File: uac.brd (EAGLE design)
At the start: 160 x 100 mm, 159 parts, among them Q1 2N7002CK4SST, Q2 2N7002CK4SST

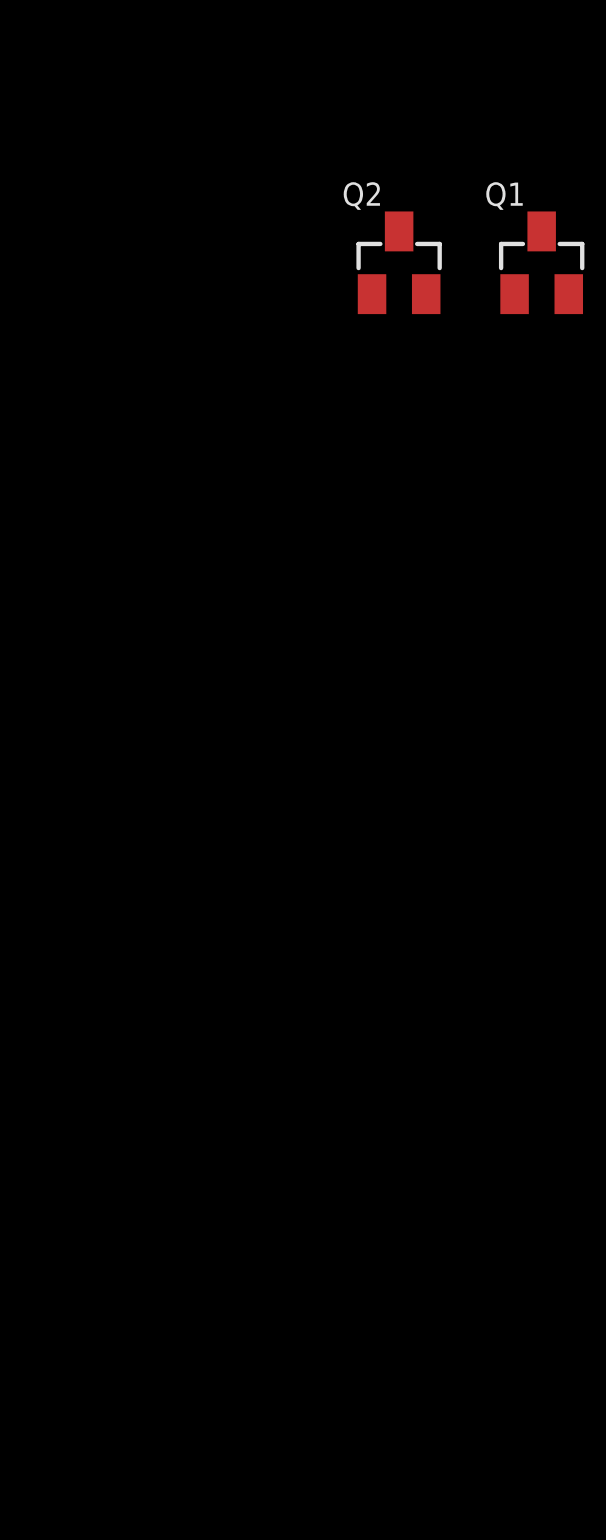
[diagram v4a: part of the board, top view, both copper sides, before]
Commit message: Leds aangesloten
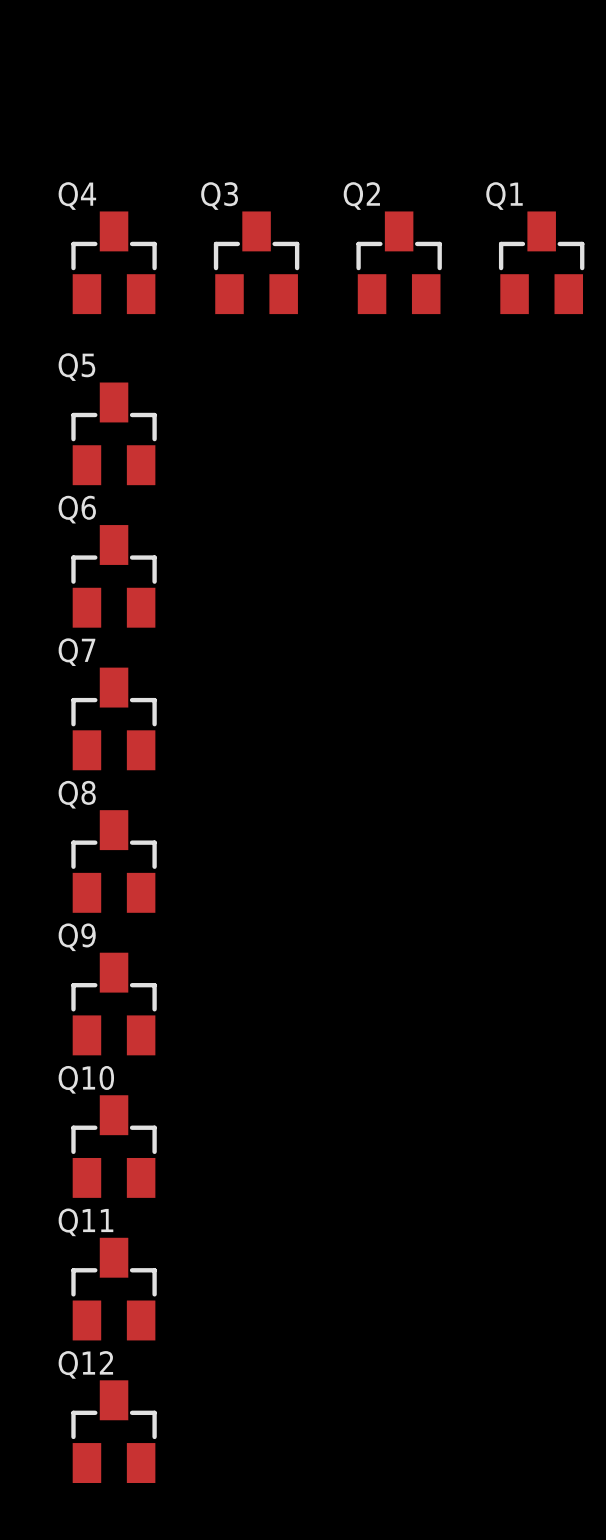
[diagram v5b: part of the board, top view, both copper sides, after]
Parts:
- added Q10, Q11, Q12, Q3, Q4, Q5, Q6, Q7, Q8, Q9: 2N7002CK4SST, Custom components:SOT23
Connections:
- new net ARCDOZEN_10: Q10.1
- new net ARCDOZEN_11: Q11.1
- new net ARCDOZEN_12: Q12.1
- new net ARCDOZEN_3: Q3.1
- new net ARCDOZEN_4: Q4.1
- new net ARCDOZEN_5: Q5.1
- new net ARCDOZEN_6: Q6.1
- new net ARCDOZEN_7: Q7.1
- new net ARCDOZEN_8: Q8.1
- new net ARCDOZEN_9: Q9.1
- new net N$10: HOUR9.C, MIN45.C, MIN46.C, MIN47.C, MIN48.C, MIN49.C, Q10.3, SEC45.C, SEC46.C, SEC47.C, SEC48.C, SEC49.C, SPECIAL9.C
- new net N$11: HOUR10.C, MIN50.C, MIN51.C, MIN52.C, MIN53.C, MIN54.C, Q11.3, SEC50.C, SEC51.C, SEC52.C, SEC53.C, SEC54.C, SPECIAL10.C
- new net N$12: HOUR11.C, MIN55.C, MIN56.C, MIN57.C, MIN58.C, MIN59.C, Q12.3, SEC55.C, SEC56.C, SEC57.C, SEC58.C, SEC59.C, SPECIAL11.C
- new net N$2: HOUR2.C, MIN10.C, MIN11.C, MIN12.C, MIN13.C, MIN14.C, Q3.3, SEC10.C, SEC11.C, SEC12.C, SEC13.C, SEC14.C, SPECIAL2.C
- new net N$4: HOUR3.C, MIN15.C, MIN16.C, MIN17.C, MIN18.C, MIN19.C, Q4.3, SEC15.C, SEC16.C, SEC17.C, SEC18.C, SEC19.C, SPECIAL3.C
- new net N$5: HOUR4.C, MIN20.C, MIN21.C, MIN22.C, MIN23.C, MIN24.C, Q5.3, SEC20.C, SEC21.C, SEC22.C, SEC23.C, SEC24.C, SPECIAL4.C
- new net N$6: HOUR5.C, MIN25.C, MIN26.C, MIN27.C, MIN28.C, MIN29.C, Q6.3, SEC25.C, SEC26.C, SEC27.C, SEC28.C, SEC29.C, SPECIAL5.C
- new net N$7: HOUR6.C, MIN30.C, MIN31.C, MIN32.C, MIN33.C, MIN34.C, Q7.3, SEC30.C, SEC31.C, SEC32.C, SEC33.C, SEC34.C, SPECIAL6.C
- new net N$8: HOUR7.C, MIN35.C, MIN36.C, MIN37.C, MIN38.C, MIN39.C, Q8.3, SEC35.C, SEC36.C, SEC37.C, SEC38.C, SEC39.C, SPECIAL7.C
- new net N$9: HOUR8.C, MIN40.C, MIN41.C, MIN42.C, MIN43.C, MIN44.C, Q9.3, SEC40.C, SEC41.C, SEC42.C, SEC43.C, SEC44.C, SPECIAL8.C
- net DOZEN1: now also HOUR10.A, HOUR11.A, HOUR2.A, HOUR3.A, HOUR4.A, HOUR5.A, HOUR6.A, HOUR7.A, HOUR8.A, HOUR9.A
- net DOZEN10: now also SEC13.A, SEC18.A, SEC23.A, SEC28.A, SEC33.A, SEC38.A, SEC43.A, SEC48.A, SEC53.A, SEC58.A
- net DOZEN11: now also SEC14.A, SEC19.A, SEC24.A, SEC29.A, SEC34.A, SEC39.A, SEC44.A, SEC49.A, SEC54.A, SEC59.A
- net DOZEN12: now also SPECIAL10.A, SPECIAL11.A, SPECIAL2.A, SPECIAL3.A, SPECIAL4.A, SPECIAL5.A, SPECIAL6.A, SPECIAL7.A, SPECIAL8.A, SPECIAL9.A
- net DOZEN2: now also MIN10.A, MIN15.A, MIN20.A, MIN25.A, MIN30.A, MIN35.A, MIN40.A, MIN45.A, MIN50.A, MIN55.A
- net DOZEN3: now also MIN11.A, MIN16.A, MIN21.A, MIN26.A, MIN31.A, MIN36.A, MIN41.A, MIN46.A, MIN51.A, MIN56.A
- net DOZEN4: now also MIN12.A, MIN17.A, MIN22.A, MIN27.A, MIN32.A, MIN37.A, MIN42.A, MIN47.A, MIN52.A, MIN57.A
- net DOZEN5: now also MIN13.A, MIN18.A, MIN23.A, MIN28.A, MIN33.A, MIN38.A, MIN43.A, MIN48.A, MIN53.A, MIN58.A
- net DOZEN6: now also MIN14.A, MIN19.A, MIN24.A, MIN29.A, MIN34.A, MIN39.A, MIN44.A, MIN49.A, MIN54.A, MIN59.A
- net DOZEN7: now also SEC10.A, SEC15.A, SEC20.A, SEC25.A, SEC30.A, SEC35.A, SEC40.A, SEC45.A, SEC50.A, SEC55.A
- net DOZEN8: now also SEC11.A, SEC16.A, SEC21.A, SEC26.A, SEC31.A, SEC36.A, SEC41.A, SEC46.A, SEC51.A, SEC56.A
- net DOZEN9: now also SEC12.A, SEC17.A, SEC22.A, SEC27.A, SEC32.A, SEC37.A, SEC42.A, SEC47.A, SEC52.A, SEC57.A
- net GND: now also Q10.2, Q11.2, Q12.2, Q3.2, Q4.2, Q5.2, Q6.2, Q7.2, Q8.2, Q9.2

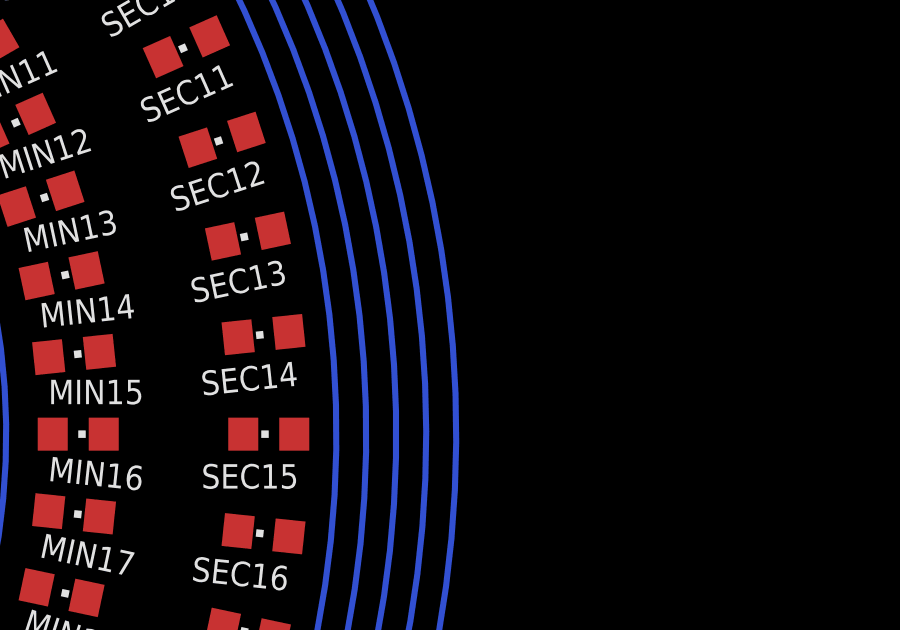
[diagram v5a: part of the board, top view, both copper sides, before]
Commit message: New via
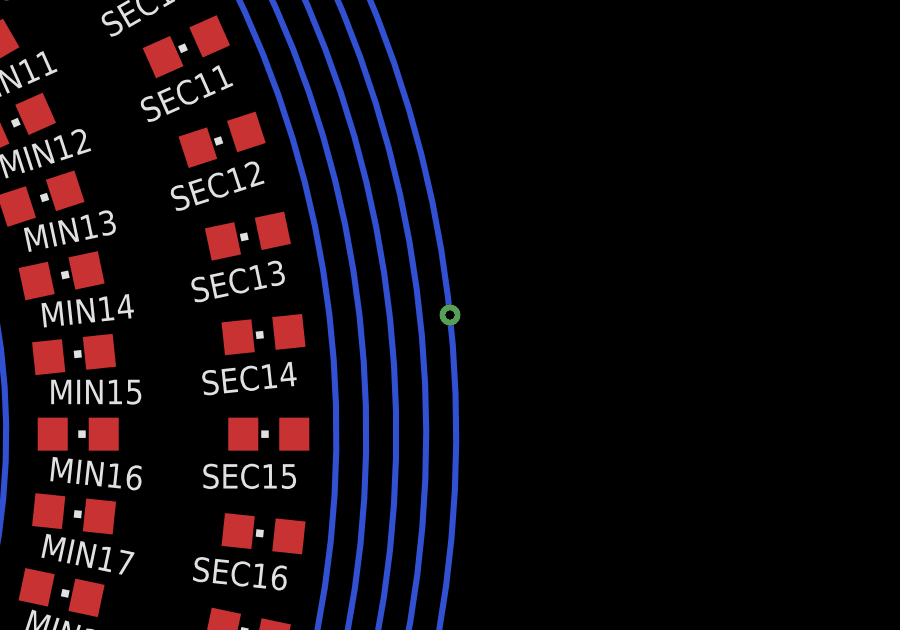
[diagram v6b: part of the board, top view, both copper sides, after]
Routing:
- net DOZEN11: vias 2 -> 3
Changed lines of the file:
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@@
 <setting verticaltext="up"/>
 </settings>
-<grid distance="1" unitdist="mm" unit="mm" style="lines" multiple="1" display="yes" altdistance="0.5" altunitdist="mm" altunit="mm"/>
+<grid distance="1" unitdist="mm" unit="mm" style="lines" multiple="1" display="yes" altdistance="0.001" altunitdist="mm" altunit="mm"/>
 <layers>
 <layer number="1" name="Top" color="4" fill="1" visible="yes" active="yes"/>
@@
 <wire x1="36.740378125" y1="20.2184125" x2="53.4076375" y2="17.578596875" width="0" layer="19" extent="1-1"/>
 <wire x1="23.62605" y1="30.8381875" x2="17.578596875" y2="46.592359375" width="0" layer="19" extent="1-1"/>
+<via x="87.79183125" y="53.97208125" extent="1-16" drill="0.3"/>
 </signal>
 <signal name="DOZEN12">

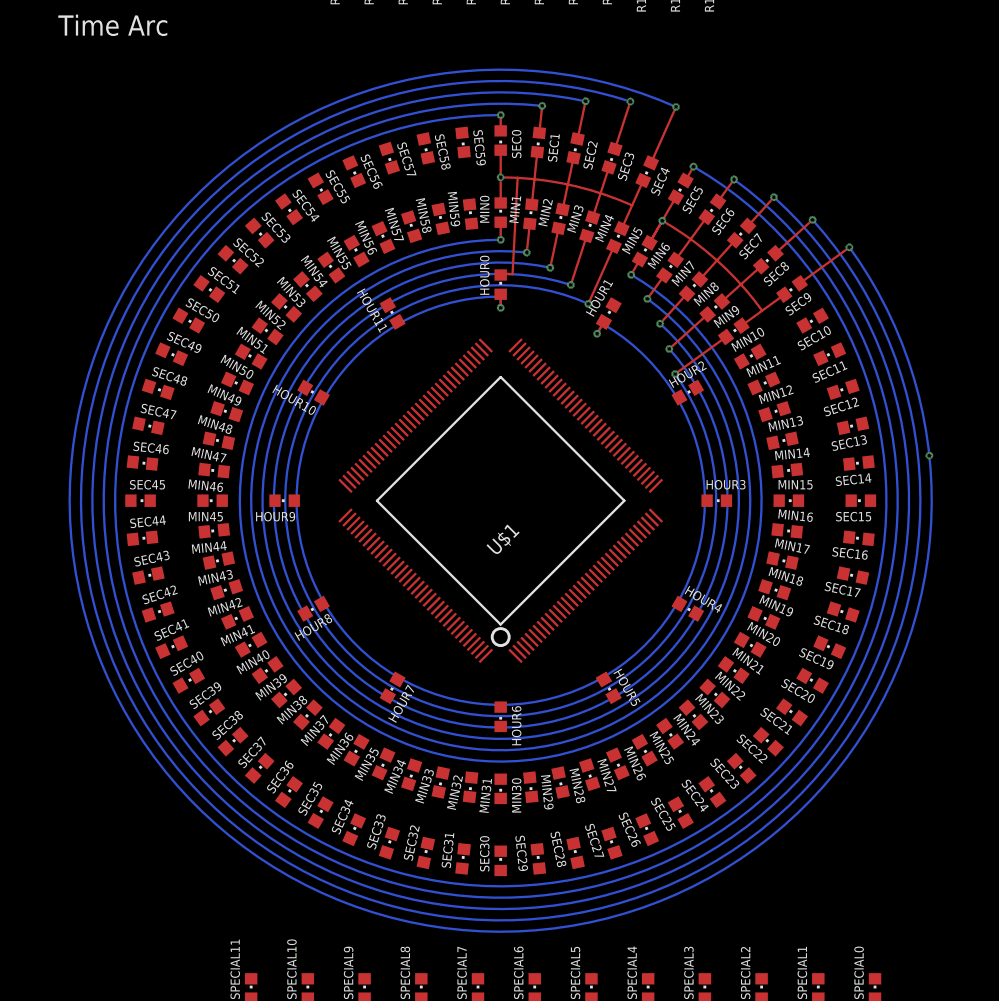
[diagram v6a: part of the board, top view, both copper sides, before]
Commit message: Outer Vias
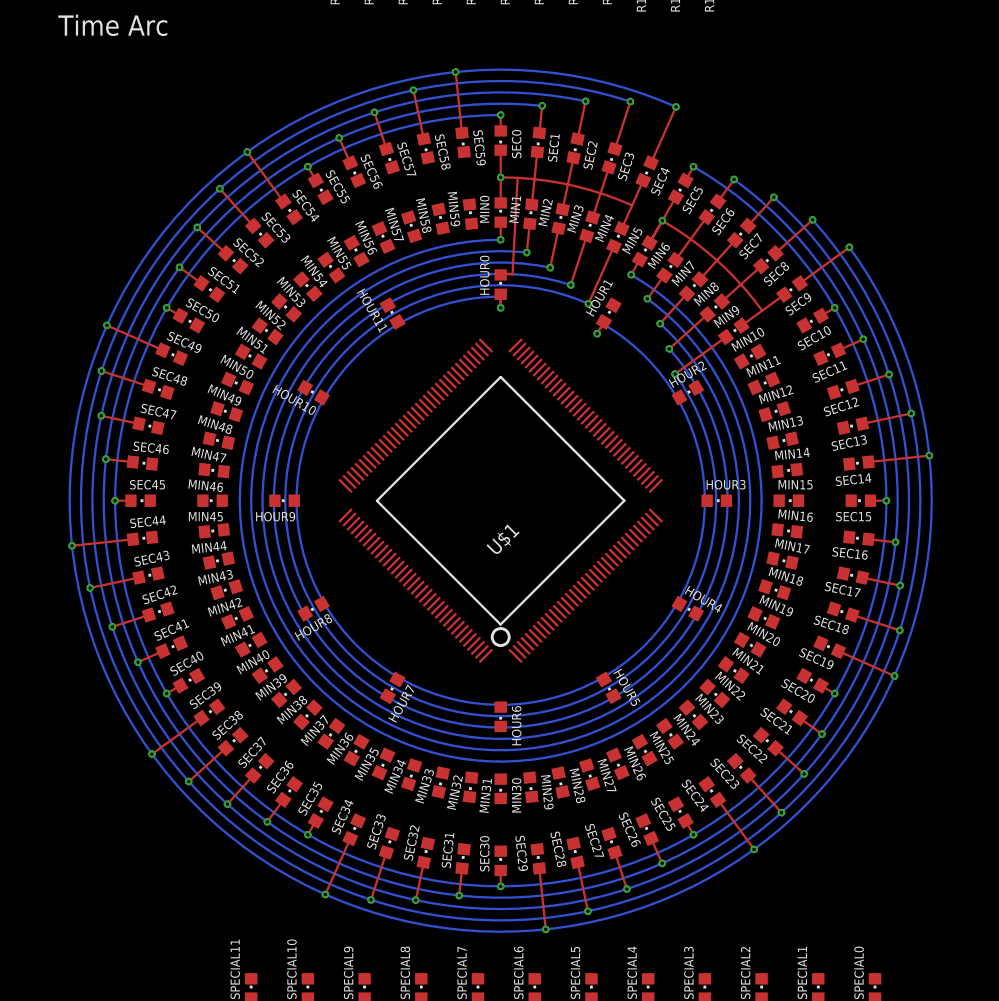
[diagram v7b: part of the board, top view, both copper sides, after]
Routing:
- net DOZEN11: track 30.5 -> 84.5 mm, vias 3 -> 12
- net DOZEN10: track 28.0 -> 72.0 mm, vias 2 -> 12
- net DOZEN9: track 25.4 -> 59.4 mm, vias 2 -> 12
- net DOZEN8: track 22.9 -> 46.9 mm, vias 2 -> 12
- net DOZEN7: track 20.4 -> 34.4 mm, vias 2 -> 12

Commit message: arcdozen arcs
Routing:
- net N$2: track 0.00 -> 16.5 mm, vias 0 -> 1
- net N$20: track 0.00 -> 11.9 mm
- net N$17: track 0.00 -> 11.9 mm
- net N$14: track 0.00 -> 11.9 mm
- net N$13: track 0.00 -> 11.9 mm
- net N$21: track 0.00 -> 11.9 mm
- net N$16: track 0.00 -> 11.9 mm
- net N$18: track 0.00 -> 11.9 mm
- net N$15: track 0.00 -> 11.9 mm
- net N$19: track 0.00 -> 11.9 mm
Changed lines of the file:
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@@
 <setting verticaltext="up"/>
 </settings>
-<grid distance="1" unitdist="mm" unit="mm" style="lines" multiple="1" display="yes" altdistance="0.001" altunitdist="mm" altunit="mm"/>
+<grid distance="1" unitdist="mm" unit="mm" style="lines" multiple="1" display="yes" altdistance="0.5" altunitdist="mm" altunit="mm"/>
 <layers>
 <layer number="1" name="Top" color="4" fill="1" visible="yes" active="yes"/>
@@
 <contactref element="SEC13" pad="C"/>
 <contactref element="SEC14" pad="C"/>
-<wire x1="78.22855625" y1="62.568165625" x2="76.760190625" y2="65.45" width="0" layer="19" extent="1-1"/>
+<via x="74.68171875" y="64.25" extent="1-16" drill="0.3"/>
+<wire x1="74.68171875" y1="64.25" x2="76.760190625" y2="65.45" width="0.2032" layer="1"/>
+<wire x1="74.68171875" y1="64.25" x2="72.733153125" y2="63.125" width="0.2032" layer="1"/>
+<wire x1="74.681725" y1="64.25" x2="78.343875" y2="52.9790625" width="0.2032" layer="1" curve="-23.999997"/>
 <wire x1="79.387653125" y1="59.54861875" x2="78.22855625" y2="62.568165625" width="0" layer="19" extent="1-1"/>
 <wire x1="80.224771875" y1="56.42448125" x2="79.387653125" y2="59.54861875" width="0" layer="19" extent="1-1"/>
-<wire x1="80.730715625" y1="53.229940625" x2="80.224771875" y2="56.42448125" width="0" layer="19" extent="1-1"/>
-<wire x1="72.733153125" y1="63.125" x2="76.760190625" y2="65.45" width="0" layer="19" extent="1-1"/>
+<wire x1="76.760190625" y1="65.45" x2="78.22855625" y2="62.568165625" width="0" layer="19" extent="1-1"/>
+<wire x1="74.681725" y1="64.25" x2="74.68171875" y2="64.25" width="0" layer="19" extent="1-1"/>
+<wire x1="76.1062" y1="52.743859375" x2="78.343875" y2="52.9790625" width="0" layer="19" extent="1-1"/>
+<wire x1="80.730715625" y1="53.229940625" x2="78.343875" y2="52.9790625" width="0" layer="19" extent="1-1"/>
 <wire x1="73.98055625" y1="60.67684375" x2="72.733153125" y2="63.125" width="0" layer="19" extent="1-1"/>
 <wire x1="74.96524375" y1="58.11169375" x2="73.98055625" y2="60.67684375" width="0" layer="19" extent="1-1"/>
-<wire x1="75.676384375" y1="55.4576875" x2="74.96524375" y2="58.11169375" width="0" layer="19" extent="1-1"/>
-<wire x1="76.1062" y1="52.743859375" x2="75.676384375" y2="55.4576875" width="0" layer="19" extent="1-1"/>
+<wire x1="75.676384375" y1="55.4576875" x2="76.1062" y2="52.743859375" width="0" layer="19" extent="1-1"/>
 <wire x1="67.2339" y1="59.95" x2="72.733153125" y2="63.125" width="0" layer="19" extent="1-1"/>
 <wire x1="73" y1="7.85" x2="76.1062" y2="52.743859375" width="0" layer="19" extent="1-1"/>
@@
 <contactref element="Q12" pad="1"/>
 </signal>
+<signal name="N$13">
+<wire x1="78.5" y1="50" x2="76.036046875" y2="38.40800625" width="0.2032" layer="1" curve="-23.999998"/>
+</signal>
+<signal name="N$14">
+<wire x1="74.681725" y1="35.75" x2="66.75188125" y2="26.943015625" width="0.2032" layer="1" curve="-23.999999"/>
+</signal>
+<signal name="N$15">
+<wire x1="64.25" y1="25.318275" x2="52.9790625" y2="21.656125" width="0.2032" layer="1" curve="-23.999997"/>
+</signal>
+<signal name="N$16">
+<wire x1="50" y1="21.5" x2="38.40800625" y2="23.963953125" width="0.2032" layer="1" curve="-23.999998"/>
+</signal>
+<signal name="N$17">
+<wire x1="35.75" y1="25.318275" x2="26.943015625" y2="33.24811875" width="0.2032" layer="1" curve="-23.999999"/>
+</signal>
+<signal name="N$18">
+<wire x1="21.656125" y1="47.0209375" x2="25.318275" y2="35.75" width="0.2032" layer="1" curve="23.999997"/>
+</signal>
+<signal name="N$19">
+<wire x1="47.0209375" y1="78.343875" x2="35.75" y2="74.681725" width="0.2032" layer="1" curve="23.999997"/>
+</signal>
+<signal name="N$20">
+<wire x1="33.24811875" y1="73.056984375" x2="25.318275" y2="64.25" width="0.2032" layer="1" curve="23.999999"/>
+</signal>
+<signal name="N$21">
+<wire x1="23.963953125" y1="61.59199375" x2="21.5" y2="50" width="0.2032" layer="1" curve="23.999998"/>
+</signal>
 </signals>
